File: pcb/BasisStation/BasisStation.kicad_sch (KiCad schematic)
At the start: 0 parts

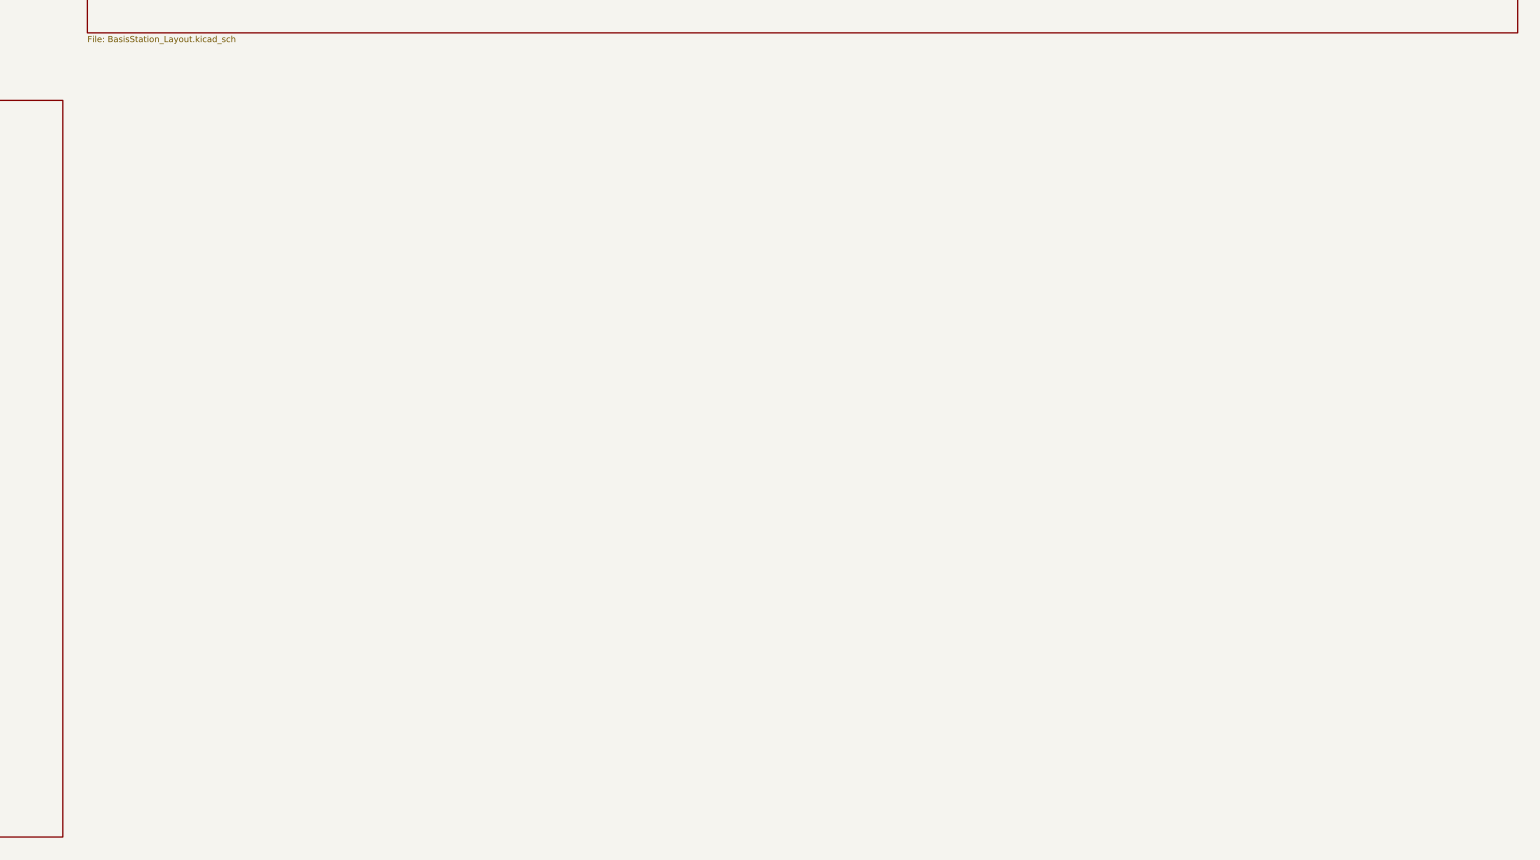
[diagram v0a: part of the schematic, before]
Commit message: v0.00.001 feat(SHBS-4): USB-C-Stromversorgung mit MP2359-Buck auf 3,3V
PS2/+12V entfernt, neue Stromversorgungs-Schaltung (Stromversorgung.kicad_sch),
Footprints fuer MP2359DJ, SOT-23-6 und USB-C-Buchse, power_supply.md als
zentrale Referenz.

Co-Authored-By: Claude Sonnet 5 <noreply@anthropic.com>
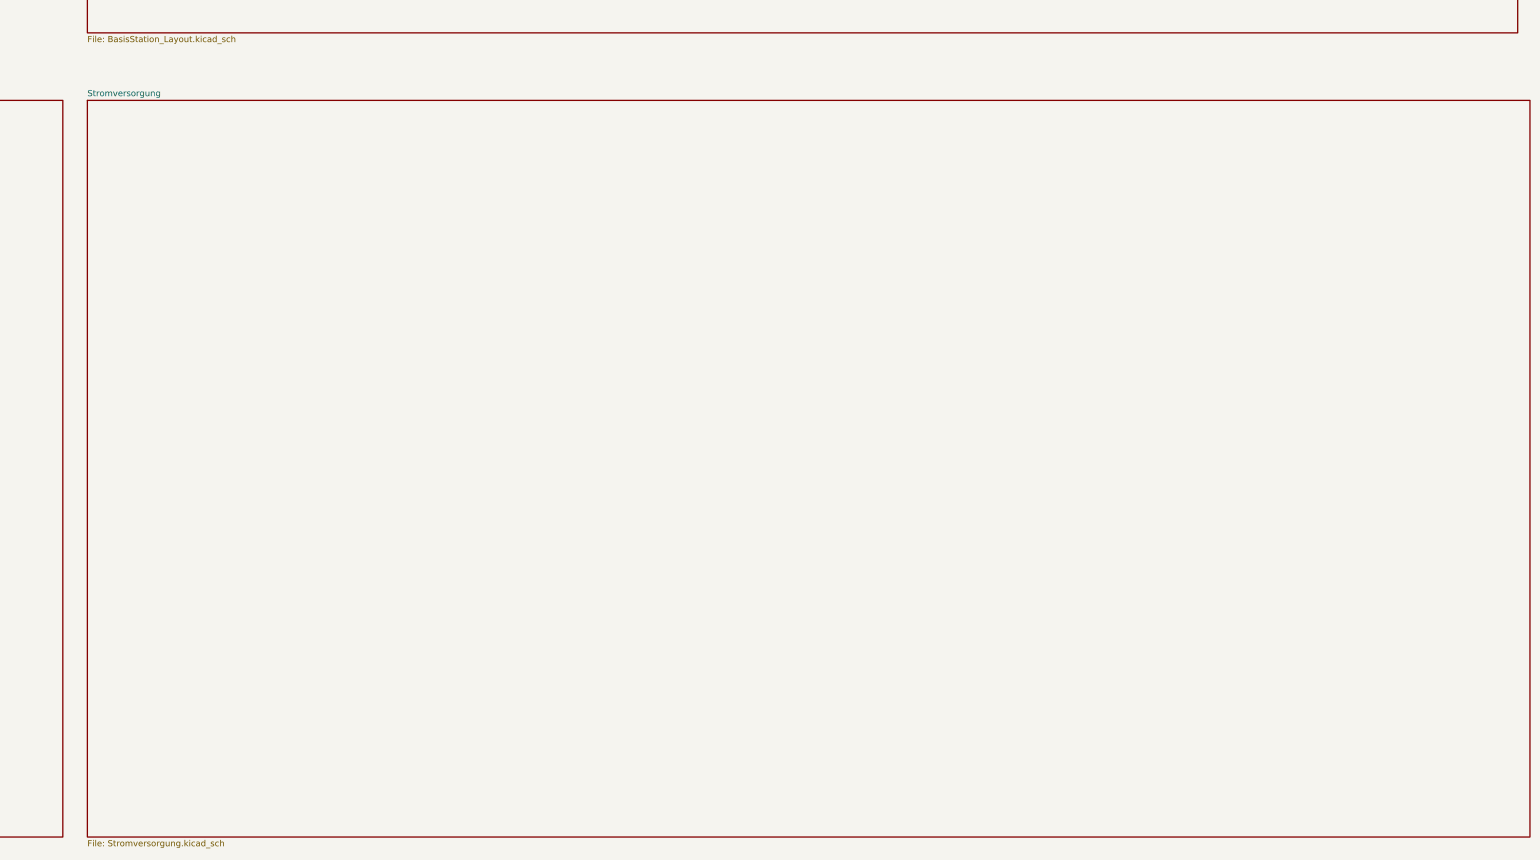
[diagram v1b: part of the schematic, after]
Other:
- added sheet Stromversorgung (Stromversorgung.kicad_sch)
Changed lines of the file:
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@@
+		)
+	)
+	(sheet
+		(at 302.26 224.79)
+		(size 298.45 152.4)
+		(exclude_from_sim no)
+		(in_bom yes)
+		(on_board yes)
+		(dnp no)
+		(fields_autoplaced yes)
+		(stroke
+			(width 0.1524)
+			(type solid)
+		)
+		(fill
+			(color 0 0 0 0.0000)
+		)
+		(property "Sheetname" "Stromversorgung"
+			(at 302.26 224.0784 0)
+			(effects
+				(font
+					(size 1.27 1.27)
+				)
+				(justify left bottom)
+			)
+		)
+		(property "Sheetfile" "Stromversorgung.kicad_sch"
+			(at 302.26 377.7746 0)
+			(effects
+				(font
+					(size 1.27 1.27)
+				)
+				(justify left top)
+			)
+		)
+		(instances
+			(project "BasisStation"
+				(path "/498c7092-55c1-4229-9f4b-13c6a8e7da47"
+					(page "4")
+				)
+			)
 		)
 	)

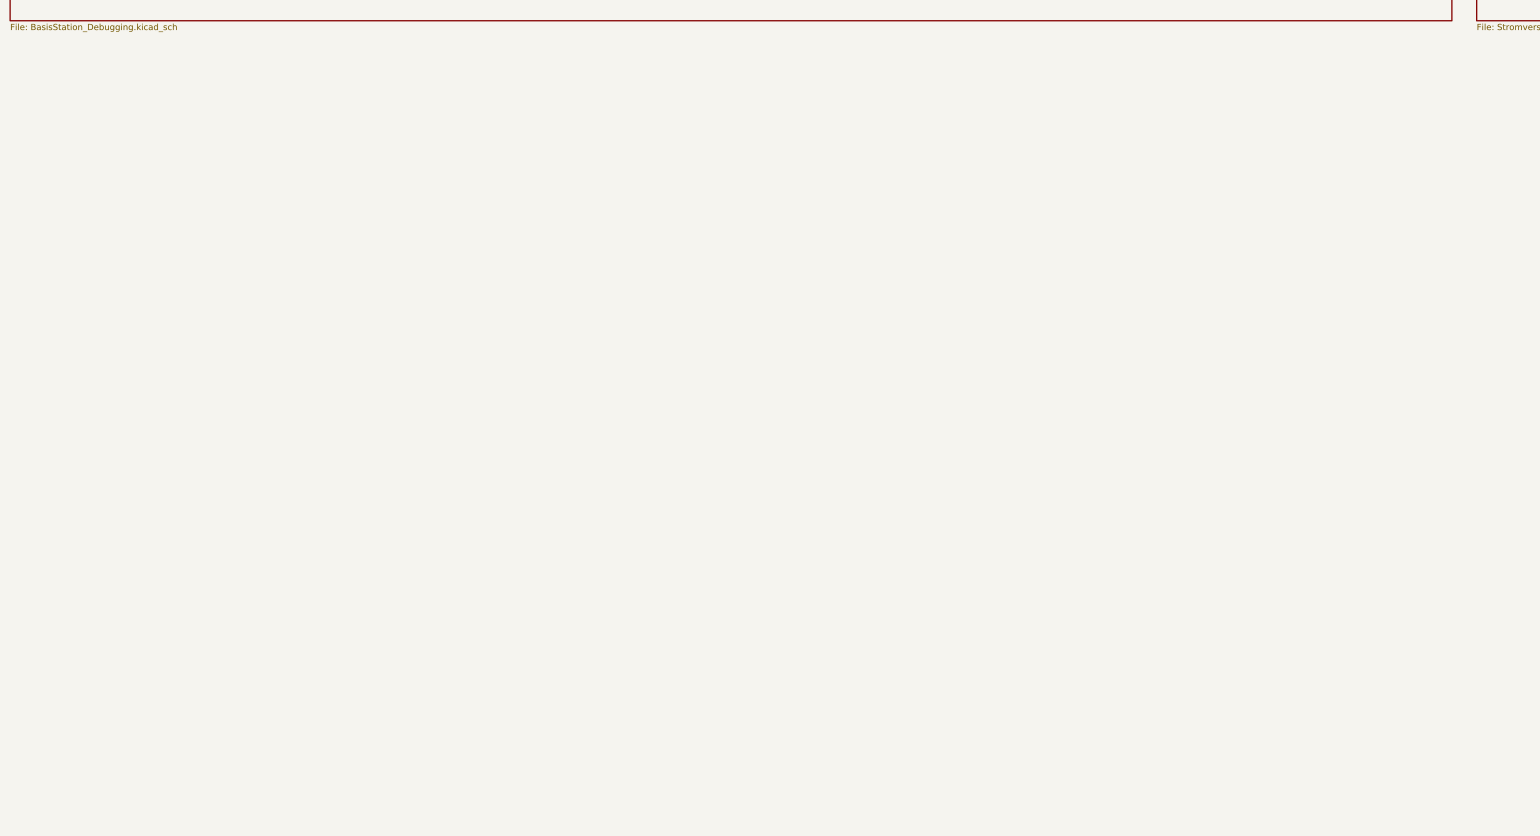
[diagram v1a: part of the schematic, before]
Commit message: v0.00.001 fix(SHBS-6): Debugging-Blatt wiederhergestellt, JTAG-Header entfaellt
Das Blatt BasisStation_Debugging.kicad_sch war beim Anlegen des neuen
Ethernet-Blatts ueberschrieben worden und enthielt nur noch einen leeren
Rumpf. Aus dem letzten Commit zurueckgeholt; J1, U1, R21 und R22 sind
wieder da. Die interne UUID stimmt mit der Referenz im Wurzelblatt
ueberein, die Annotation bleibt damit erhalten.

Der 10-polige JTAG-Header J5 wurde bewusst entfernt: Der ESP32-S3 bringt
USB-Serial-JTAG im Chip mit, On-Chip-Debugging laeuft ueber J1. Das spart
einen Steckverbinder und dessen Platinenflaeche.

Doku nachgezogen: Schnittstellentabelle in hardware.md, Begruendung der
LED-Pinwahl (GPIO3 bleibt aus Strapping-Gruenden unbelegt, auch ohne J5),
sowie der GPIO-Ausschluss in Task 0003.

Offen: Das Board enthaelt den Footprint von J5 noch, er verschwindet beim
naechsten Netzlisten-Import.

Co-Authored-By: Claude Opus 5 <noreply@anthropic.com>
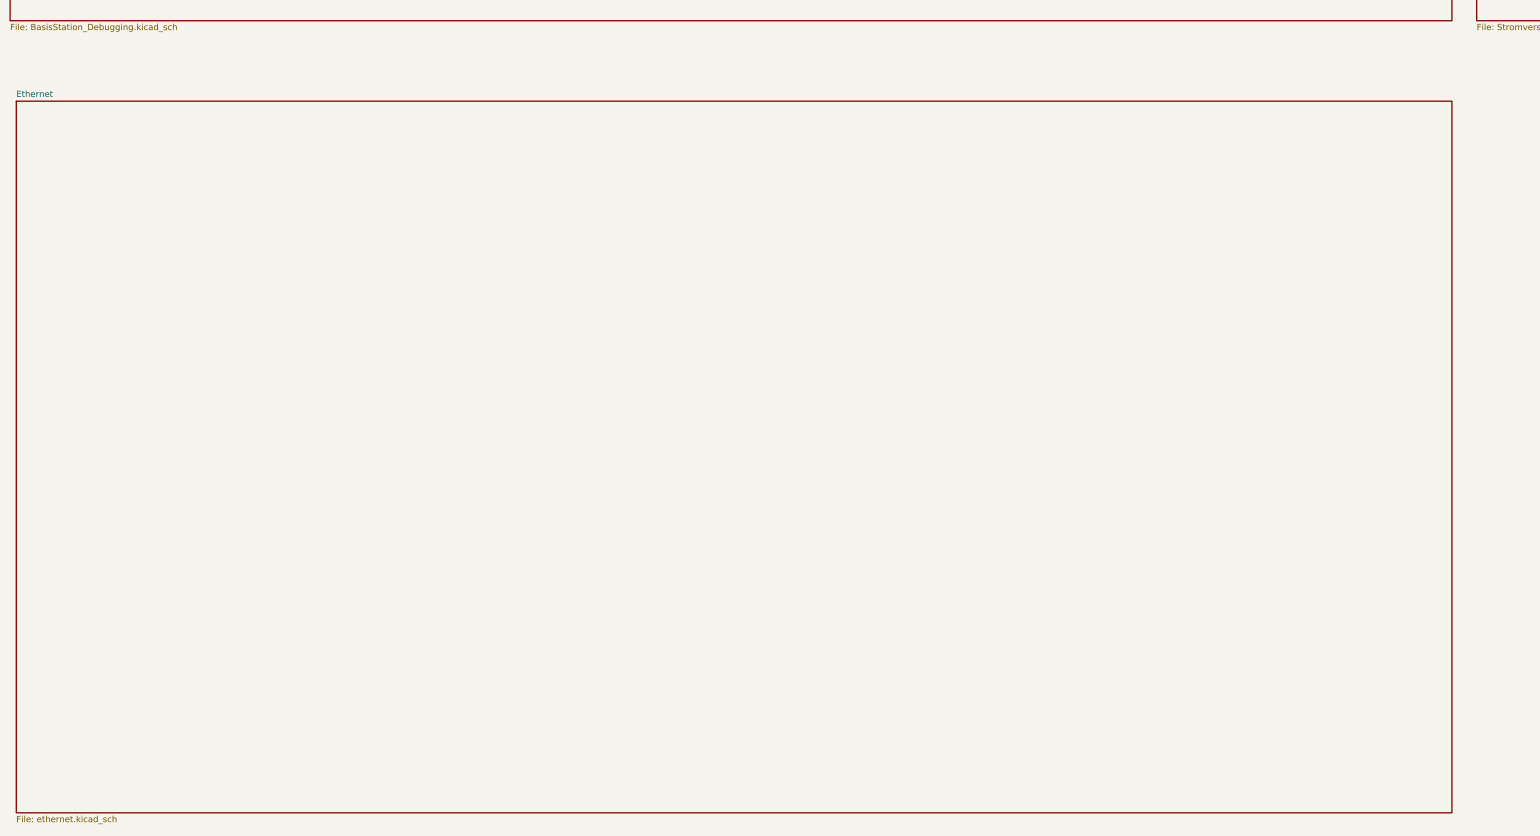
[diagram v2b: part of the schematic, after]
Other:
- added sheet Ethernet (ethernet.kicad_sch)
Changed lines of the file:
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@@
+	)
+	(sheet
+		(at 2.54 393.7)
+		(size 294.64 146.05)
+		(exclude_from_sim no)
+		(in_bom yes)
+		(on_board yes)
+		(dnp no)
+		(fields_autoplaced yes)
+		(stroke
+			(width 0.1524)
+			(type solid)
+		)
+		(fill
+			(color 0 0 0 0.0000)
+		)
+		(property "Sheetname" "Ethernet"
+			(at 2.54 392.9884 0)
+			(effects
+				(font
+					(size 1.27 1.27)
+				)
+				(justify left bottom)
+			)
+		)
+		(property "Sheetfile" "ethernet.kicad_sch"
+			(at 2.54 540.3346 0)
+			(effects
+				(font
+					(size 1.27 1.27)
+				)
+				(justify left top)
+			)
+		)
+		(instances
+			(project "BasisStation"
+				(path "/498c7092-55c1-4229-9f4b-13c6a8e7da47"
+					(page "5")
+				)
+			)
+		)
 	)
 	(sheet
